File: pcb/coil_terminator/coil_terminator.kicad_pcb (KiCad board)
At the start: 2 copper layers, 11.2 x 5 mm, 2 parts, among them J1 Conn_Coaxial

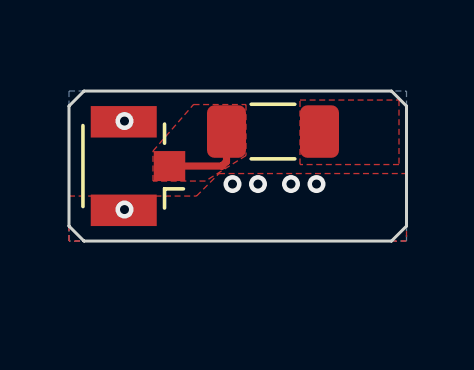
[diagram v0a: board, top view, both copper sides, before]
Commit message: added models for compensating coil loss
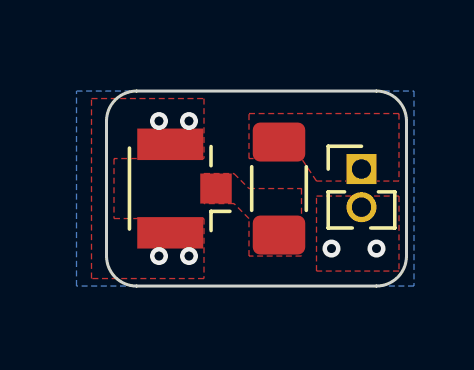
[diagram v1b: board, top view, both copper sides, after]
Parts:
- added J2: Conn_01x02_Male, Connector_PinHeader_1.27mm:PinHeader_1x02_P1.27mm_Vertical, F.Cu at (116.5, 110.3)
- moved R1 1.91 mm to (113.8, 111.0), turned to -90 degrees
- moved J1 1.72 mm to (110.6, 111.0)
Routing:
- net Net-(J1-Pad1): track 2.96 -> 0.00 mm
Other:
- board size 11.2 x 5 mm -> 10 x 6.5 mm
- board text removed: "JLCJLCJLCJLC"

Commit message: next revision
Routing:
- net GND: vias 6 -> 5
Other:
- board size 10 x 6.5 mm -> 11 x 7.5 mm
- board text added: "+"
- board text added: "-"
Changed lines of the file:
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@@
     )
     (fp_line (start -1.11 0) (end -1.11 -0.76) (layer "F.SilkS") (width 0.12))
-    (fp_line (start 0.563471 0.76) (end 1.11 0.76) (layer "F.SilkS") (width 0.12))
     (fp_line (start -1.11 1.965) (end -0.30753 1.965) (layer "F.SilkS") (width 0.12))
-    (fp_line (start 1.11 0.76) (end 1.11 1.965) (layer "F.SilkS") (width 0.12))
-    (fp_line (start 0.30753 1.965) (end 1.11 1.965) (layer "F.SilkS") (width 0.12))
     (fp_line (start -1.11 0.76) (end -0.563471 0.76) (layer "F.SilkS") (width 0.12))
     (fp_line (start -1.11 0.76) (end -1.11 1.965) (layer "F.SilkS") (width 0.12))
@@
     )
   )
-  (gr_rect (start 115.25 111.25) (end 117.75 113.75) (layer "F.Mask") (width 0.15) (fill solid))
-  (gr_rect (start 115.25 110.75) (end 117.75 108.5) (layer "F.Mask") (width 0.15) (fill solid))
-  (gr_arc (start 108 108.75) (mid 108.292893 108.042893) (end 109 107.75) (layer "Edge.Cuts") (width 0.1))
-  (gr_arc (start 118 113.25) (mid 117.707107 113.957107) (end 117 114.25) (layer "Edge.Cuts") (width 0.1))
-  (gr_line (start 118 113.25) (end 118 108.75) (layer "Edge.Cuts") (width 0.1))
-  (gr_line (start 108 108.75) (end 108 113.25) (layer "Edge.Cuts") (width 0.1))
-  (gr_line (start 117 107.75) (end 109 107.75) (layer "Edge.Cuts") (width 0.1))
-  (gr_line (start 109 114.25) (end 117 114.25) (layer "Edge.Cuts") (width 0.1))
-  (gr_arc (start 117 107.75) (mid 117.707107 108.042893) (end 118 108.75) (layer "Edge.Cuts") (width 0.1))
-  (gr_arc (start 109 114.25) (mid 108.292893 113.957107) (end 108 113.25) (layer "Edge.Cuts") (width 0.1))
+  (gr_rect (start 115.25 111.25) (end 117.25 113.75) (layer "F.Mask") (width 0.15) (fill solid))
+  (gr_rect (start 115.25 110.75) (end 117.25 108.5) (layer "F.Mask") (width 0.15) (fill solid))
+  (gr_line (start 117.5 114.75) (end 117.5 107.25) (layer "Edge.Cuts") (width 0.1))
+  (gr_line (start 106.5 107.25) (end 106.5 114.75) (layer "Edge.Cuts") (width 0.1))
+  (gr_line (start 117.5 107.25) (end 106.5 107.25) (layer "Edge.Cuts") (width 0.1))
+  (gr_line (start 106.5 114.75) (end 117.5 114.75) (layer "Edge.Cuts") (width 0.1))
   (gr_line (start 113.25 111) (end 117.55 111) (layer "User.2") (width 0.15))
+  (gr_text "-" (at 116.25 114) (layer "F.SilkS")
+    (effects (font (size 1 1) (thickness 0.15)))
+  )
+  (gr_text "+" (at 116 107.75) (layer "F.SilkS")
+    (effects (font (size 1 1) (thickness 0.15)))
+  )
   (via (at 109.75 113.25) (size 0.6) (drill 0.3) (layers "F.Cu" "B.Cu") (free) (net 2))
   (via (at 110.75 108.75) (size 0.6) (drill 0.3) (layers "F.Cu" "B.Cu") (free) (net 2))
-  (via (at 115.5 113) (size 0.6) (drill 0.3) (layers "F.Cu" "B.Cu") (free) (net 2))
+  (via (at 116.25 113.25) (size 0.6) (drill 0.3) (layers "F.Cu" "B.Cu") (free) (net 2))
   (via (at 109.75 108.75) (size 0.6) (drill 0.3) (layers "F.Cu" "B.Cu") (free) (net 2))
   (via (at 110.75 113.25) (size 0.6) (drill 0.3) (layers "F.Cu" "B.Cu") (free) (net 2))
-  (via (at 117 113) (size 0.6) (drill 0.3) (layers "F.Cu" "B.Cu") (free) (net 2))
   (zone (net 3) (net_name "/coil") (layer "F.Cu") (hatch edge 0.508)
     (priority 1)
@@
     (polygon
       (pts
-        (xy 117.75 110.75)
+        (xy 117.25 110.75)
         (xy 115 110.75)
         (xy 114.5 110)
         (xy 112.75 110)
         (xy 112.75 108.5)
-        (xy 117.75 108.5)
+        (xy 117.25 108.5)
       )
     )
@@
         (xy 108.25 112)
         (xy 111.25 112)
-        (xy 111.25 114)
-        (xy 107.5 114)
-        (xy 107.5 108)
-        (xy 111.25 108)
+        (xy 111.25 114.65)
+        (xy 106.6 114.65)
+        (xy 106.6 107.35)
+        (xy 111.25 107.35)
       )
     )
@@
     (polygon
       (pts
-        (xy 117.75 113.75)
+        (xy 117.25 113.75)
         (xy 115 113.75)
         (xy 115 111.25)
-        (xy 117.75 111.25)
+        (xy 117.25 111.25)
       )
     )
@@
     (polygon
       (pts
-        (xy 118.25 114.25)
-        (xy 107 114.25)
-        (xy 107 107.75)
-        (xy 118.25 107.75)
+        (xy 117.4 114.65)
+        (xy 106.6 114.65)
+        (xy 106.6 107.35)
+        (xy 117.4 107.35)
       )
     )
